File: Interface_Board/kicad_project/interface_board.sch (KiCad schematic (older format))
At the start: 37 parts, among them J1 INPUT, J2 Conn_01x12, J3 Conn_01x12, SW1 RESET, U1 TPS563200, U2 TPS563200, U3 PCA9600DP, U4 MCP23008SS, U5 SC18IS602B

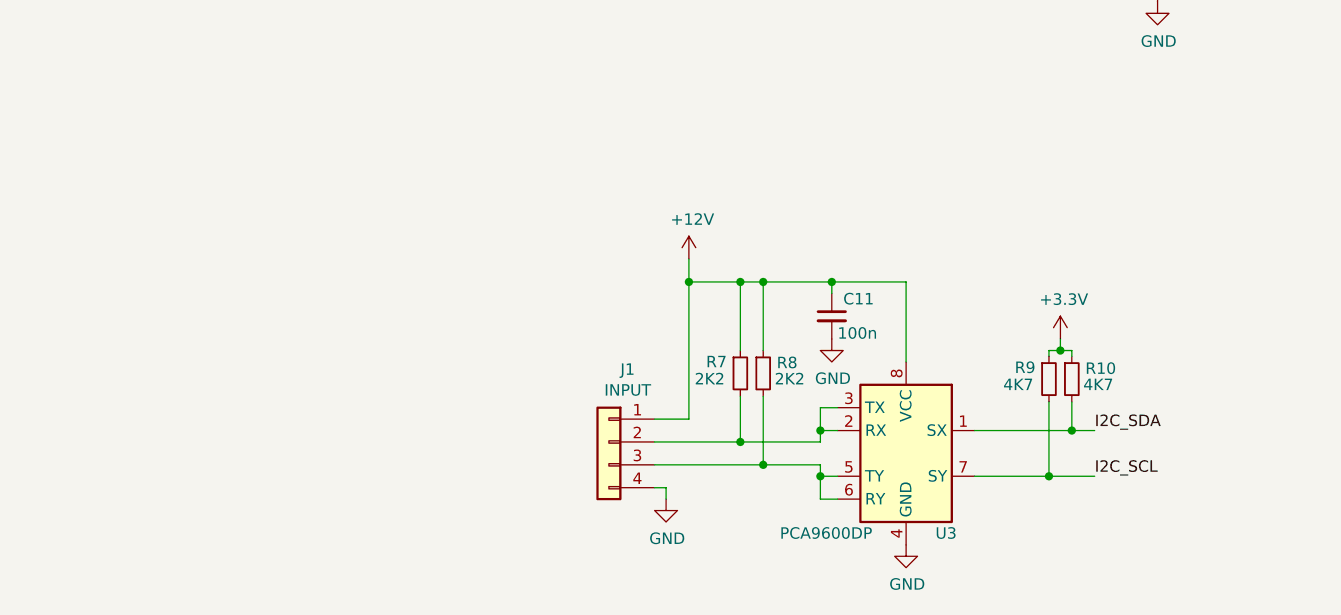
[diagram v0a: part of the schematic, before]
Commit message: add input protection to interface board
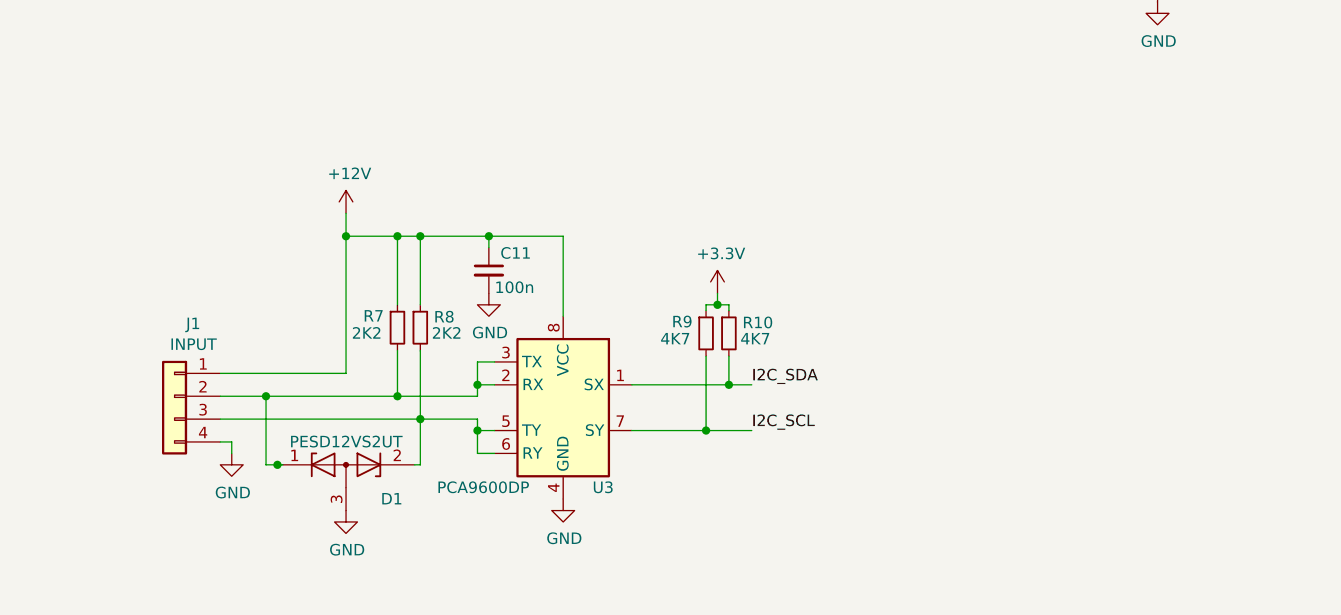
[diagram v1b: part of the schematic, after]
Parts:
- added D1: PESD12VS2UT, Package_TO_SOT_SMD:SOT-23, symbol Device:D_Zener_x2_ACom_KKA
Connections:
- net GND: now also D1.3 (A)
- net at J1.2 (Pin_2), R7.2, U3.2 (RX)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: now also D1.1 (K)
- net at J1.3 (Pin_3), R8.2, U3.5 (TY)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: now also D1.2 (K)
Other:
- moved on the sheet: C11, J1, R10, R7, R8, R9, U3

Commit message: change connector for interface board, edit silkscreen layers for interface and main boards
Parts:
- J1: footprint Connector_PinHeader_2.54mm:PinHeader_1x04_P2.54mm_Vertical -> LoaDy:Molex_70543-0003
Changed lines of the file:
@@
 encoding utf-8
 Sheet 1 1
-Title "Cube Interface Board"
-Date ""
-Rev "1"
-Comp ""
-Comment1 "Olřich Pecák"
+Title "Cube Interface Board - Schematic"
+Date "2020-10-18"
+Rev "2"
+Comp "Olřich Pecák (LoaDy)"
+Comment1 "Licensed under CERN-OHL-W v2"
 Comment2 ""
 Comment3 ""
@@
 F 0 "J1" H 2143 5342 50  0000 C CNN
 F 1 "INPUT" H 2143 5251 50  0000 C CNN
-F 2 "Connector_PinHeader_2.54mm:PinHeader_1x04_P2.54mm_Vertical" H 2225 5025 50  0001 C CNN
+F 2 "LoaDy:Molex_70543-0003" H 2225 5025 50  0001 C CNN
 F 3 "~" H 2225 5025 50  0001 C CNN
 	1    2225 5025
